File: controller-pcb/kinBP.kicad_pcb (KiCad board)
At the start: 2 copper layers, 100 x 86.3 mm, 31 parts, among them J1 LEFT_TOP, J10 LEFT_THUMB, J11 RIGHT_THUMB, J14 Conn_02x04_Odd_Even, J15 USB Cable Socket, J2 LEFT_TOP, J3 RIGHT_TOP, J4 RIGHT_TOP, J5 RIGHT_KEYWELL, J6 LEFT_KEYWELL, J7 LEFT_THUMB, J8 RIGHT_THUMB, J9 Conn_02x04_Odd_Even, Q1 MMBT3904, Q2 MMBT3904, U1 weact_STM32F4x1

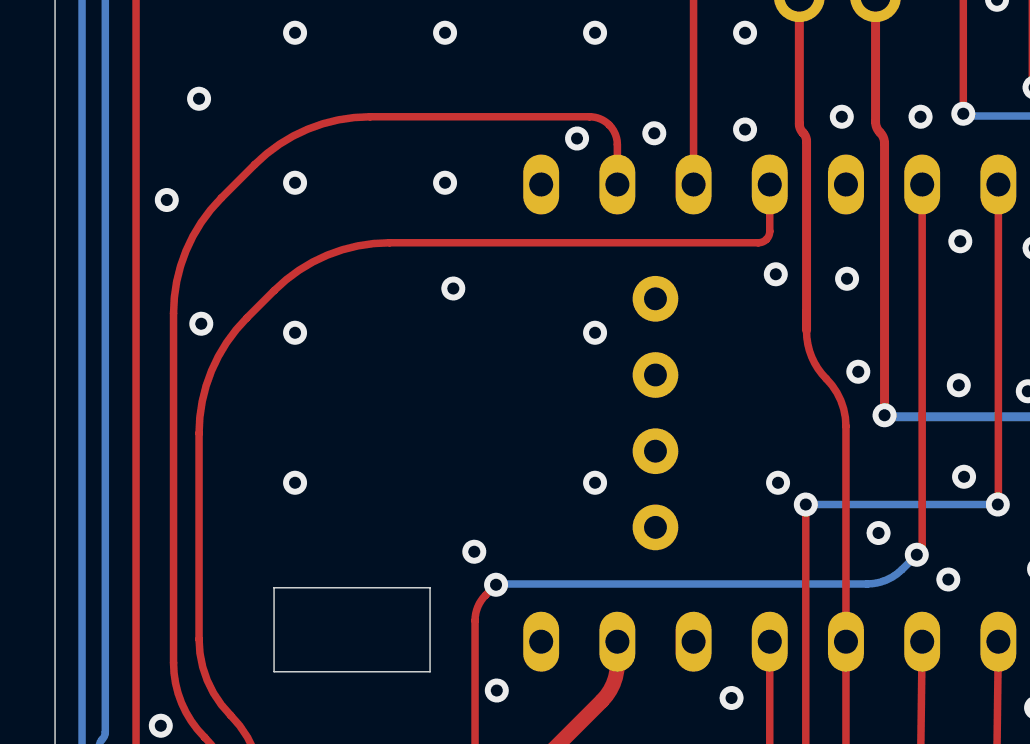
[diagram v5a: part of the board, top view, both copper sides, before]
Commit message: Added 10pin ARM Cortex debug header.
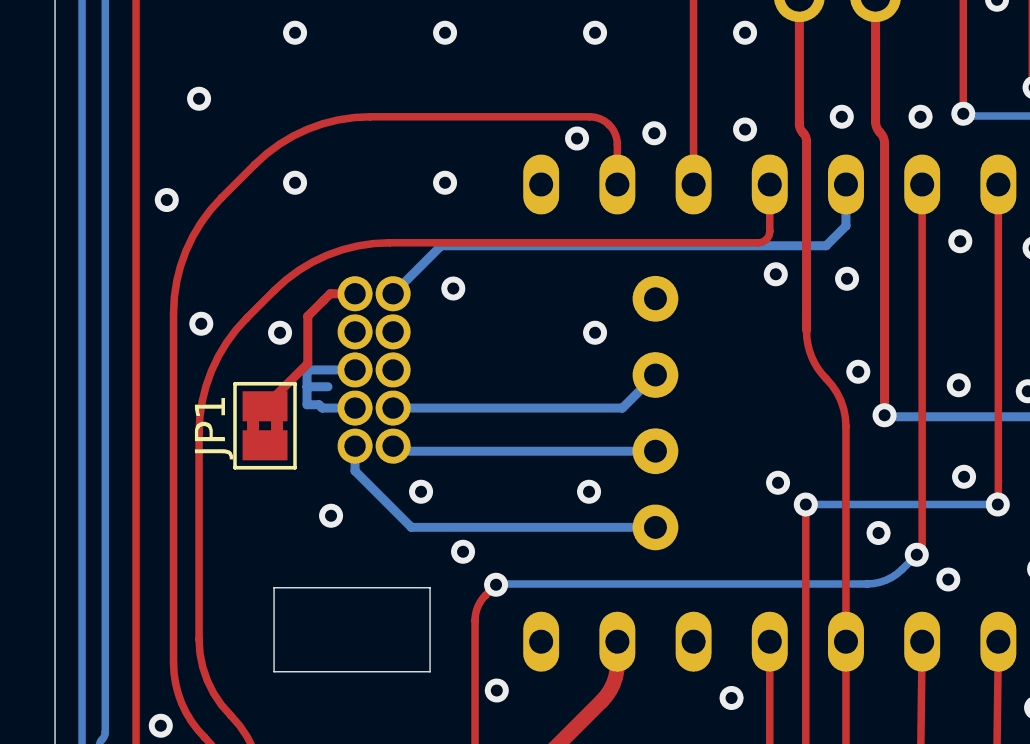
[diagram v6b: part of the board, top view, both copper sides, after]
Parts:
- added J10: Conn_ARM_JTAG_SWD_10, river:CONN_3220-10-0100-00_CNC, B.Cu at (92.0, 96.3)
- added JP1: Jumper_2_Bridged, Jumper:SolderJumper-2_P1.3mm_Bridged2Bar_Pad1.0x1.5mm, F.Cu at (89.0, 95.6)
- R3: renamed from R2; value R -> 3k3
- R4: renamed from R3; value R -> 3k3
- renumbered J3 to J1, J10 to J11, J11 to J12, J14 to J13, J9 to J16, J4 to J2, J1 to J3, J2 to J4, J15 to J9, R4 to R1, R9 to R2
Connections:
- U1 pad 20: +3V3 -> unconnected-(U1-3V3-Pad20)
- U1 pad 25: unconnected-(U1-RST-Pad25) -> SRST
- U1 pad 41: unconnected-(U1-3V3-Pad41) -> +3V3
- U1 pad 42: unconnected-(U1-A13-Pad42) -> TMS
- U1 pad 43: unconnected-(U1-A14-Pad43) -> TCK
- U1 pad 44: unconnected-(U1-GND-Pad44) -> GND
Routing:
- net SRST: track 0.00 -> 17.4 mm
- net +3V3: track 0.00 -> 11.6 mm
- net TCK: track 0.00 -> 9.20 mm
- net TMS: track 0.00 -> 8.81 mm
- net Net-(J10-GNDDetect): track 0.00 -> 5.48 mm
- net GND: track 188.0 -> 193.2 mm, vias 372 -> 373
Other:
- board text added: "Cortex Debug"
